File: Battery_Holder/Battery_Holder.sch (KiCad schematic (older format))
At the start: 1 part

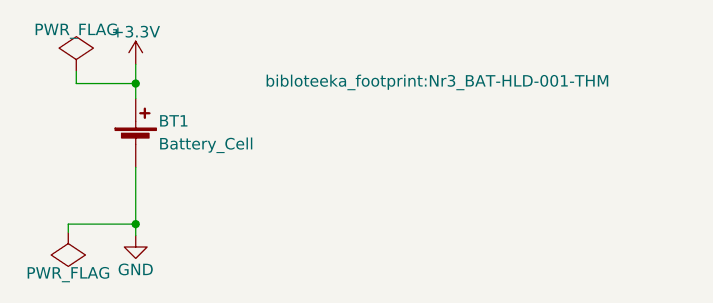
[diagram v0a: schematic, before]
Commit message: izlaboju kludu PWR un papildijnaju battery holder ar kontuuram
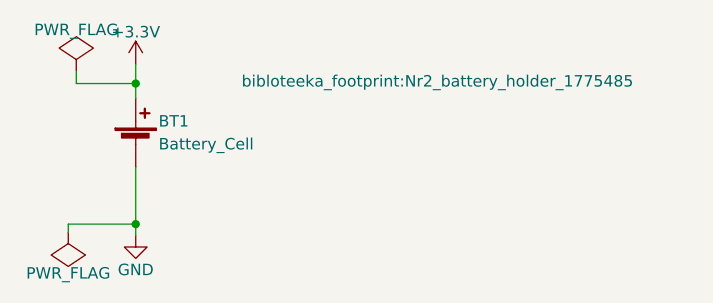
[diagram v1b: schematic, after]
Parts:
- BT1: footprint bibloteeka_footprint:Nr3_BAT-HLD-001-THM -> bibloteeka_footprint:Nr2_battery_holder_1775485
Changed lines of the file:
@@
 F 0 "BT1" H 3650 3200 50  0000 L CNN
 F 1 "Battery_Cell" H 3650 3100 50  0000 L CNN
-F 2 "bibloteeka_footprint:Nr3_BAT-HLD-001-THM" H 4870 3375 50  0000 C CNN
+F 2 "bibloteeka_footprint:Nr2_battery_holder_1775485" H 4870 3375 50  0000 C CNN
 F 3 "" V 3550 3160 50  0000 C CNN
 	1    3550 3100
